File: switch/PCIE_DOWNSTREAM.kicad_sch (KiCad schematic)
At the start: 1 part, among them J2 Bus_PCI_Express_x1

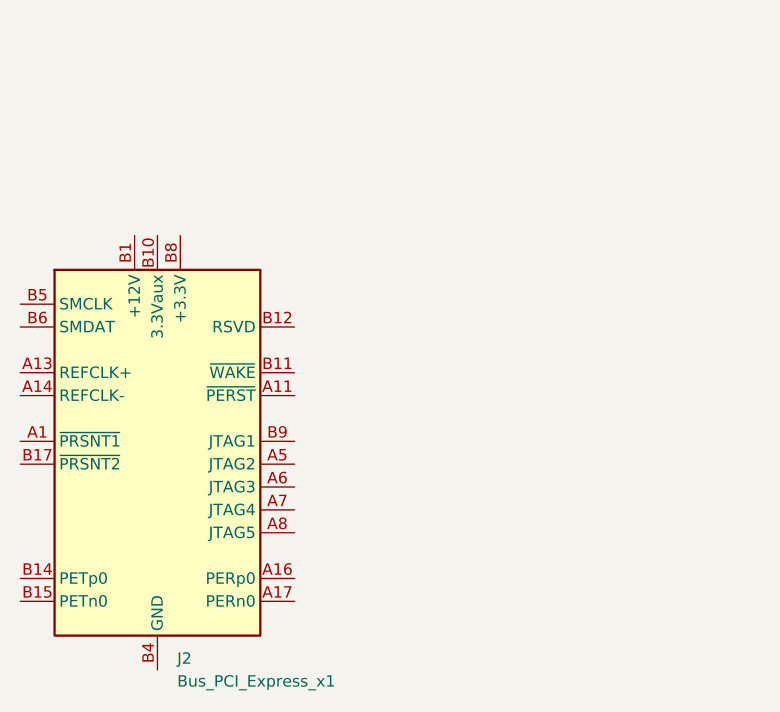
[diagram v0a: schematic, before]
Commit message: Working on power supplies.
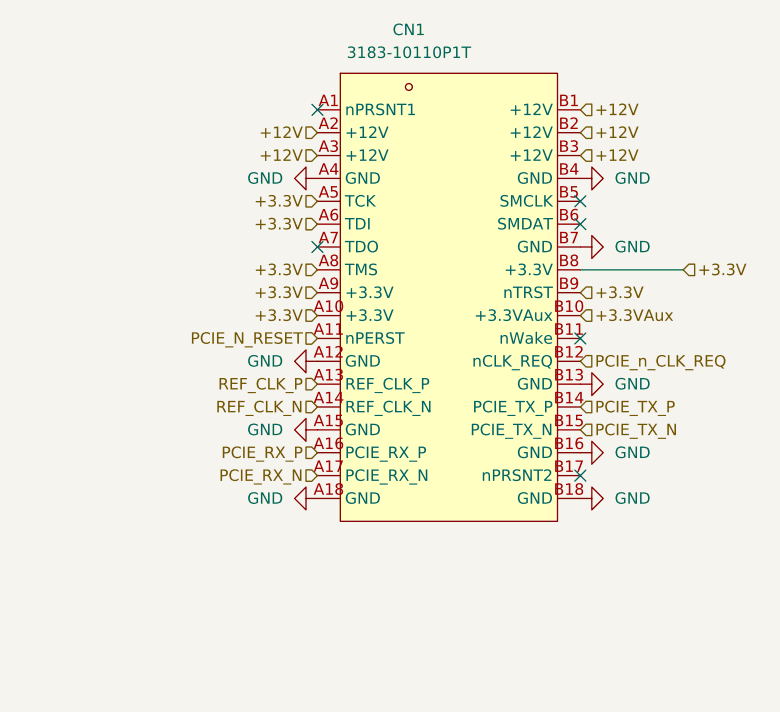
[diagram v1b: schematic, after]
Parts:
- removed J2: Bus_PCI_Express_x1, Connector_PCBEdge:BUS_PCIexpress_x1, symbol Connector:Bus_PCI_Express_x1
- added CN1: 3183-10110P1T, NEW:CONN-TH_36P-P1.00-V_3183-XXXXXPXT, symbol NEW:3183-10110P1T
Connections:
- new net +12V: CN1.A2 (+12V), CN1.A3 (+12V), CN1.B1 (+12V), CN1.B2 (+12V), CN1.B3 (+12V)
- new net +3.3V: CN1.A10 (+3.3V), CN1.A5 (TCK), CN1.A6 (TDI), CN1.A8 (TMS), CN1.A9 (+3.3V), CN1.B8 (+3.3V), CN1.B9 (nTRST)
- new net +3.3VAux: CN1.B10 (+3.3VAux)
- new net GND: CN1.A12 (GND), CN1.A15 (GND), CN1.A18 (GND), CN1.A4 (GND), CN1.B13 (GND), CN1.B16 (GND), CN1.B18 (GND), CN1.B4 (GND), CN1.B7 (GND)
- new net PCIE_N_RESET: CN1.A11 (nPERST)
- new net PCIE_RX_N: CN1.A17 (PCIE_RX_N)
- new net PCIE_RX_P: CN1.A16 (PCIE_RX_P)
- new net PCIE_TX_N: CN1.B15 (PCIE_TX_N)
- new net PCIE_TX_P: CN1.B14 (PCIE_TX_P)
- new net PCIE_n_CLK_REQ: CN1.B12 (nCLK_REQ)
- new net REF_CLK_N: CN1.A14 (REF_CLK_N)
- new net REF_CLK_P: CN1.A13 (REF_CLK_P)
- no-connect marks 0 -> 6
